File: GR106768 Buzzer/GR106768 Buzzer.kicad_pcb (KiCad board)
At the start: 4 copper layers, 76 x 58 mm, 232 parts, among them IC1 L-BC-SOT23-5, IC2 L-BC-SO08, IC3 L-BC-SO08, IC4 L-BC-SOT23-5, IC5 L-BC-SO08, IC6 L-BC-SO08, IC7 L-BC-SOT23-6, IC8 L-BC-DFN10, IC9 L-BC-SOT23-6, J1 BAR-10-1007, J2 MIRECMS, J3 MIRECMS, SW1 SI-10-NK236, T1 Q-BC-SOT23-BEC, T10 Q-BC-SOT23-GSD, T11 Q-BC-SOT23-GSD, T12 Q-BC-SOT23-GSD, T13 Q-BC-SOT23-GSD, T2 Q-BC-SOT23-BEC, T3 Q-BC-SOT23-BEC, T4 Q-BC-SOT23-BEC, T5 Q-BC-SOT23-GSD, T6 Q-BC-SOT23-GSD, T7 Q-BC-SOT23-GSD, T8 Q-BC-SOT23-GSD, T9 Q-BC-SOT23-GSD

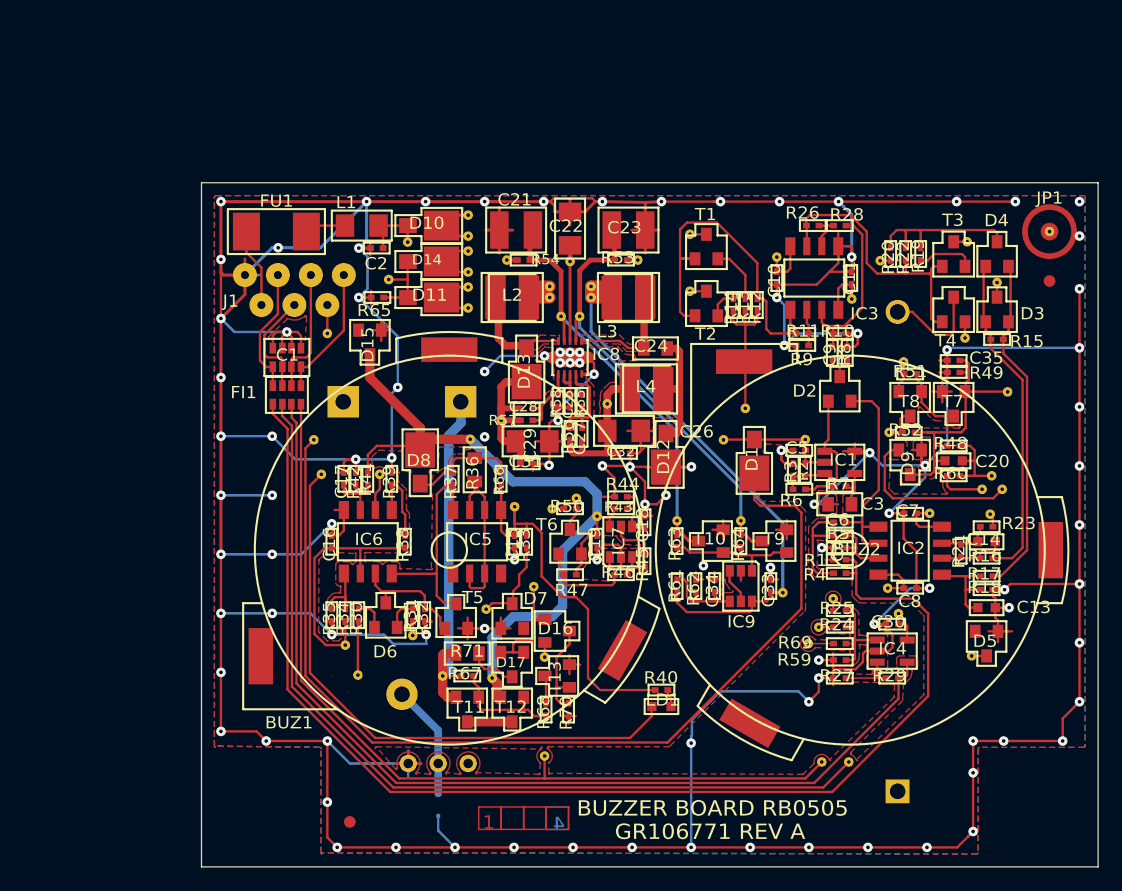
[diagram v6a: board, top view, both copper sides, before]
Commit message: buzzer pcb, schematics, etc.
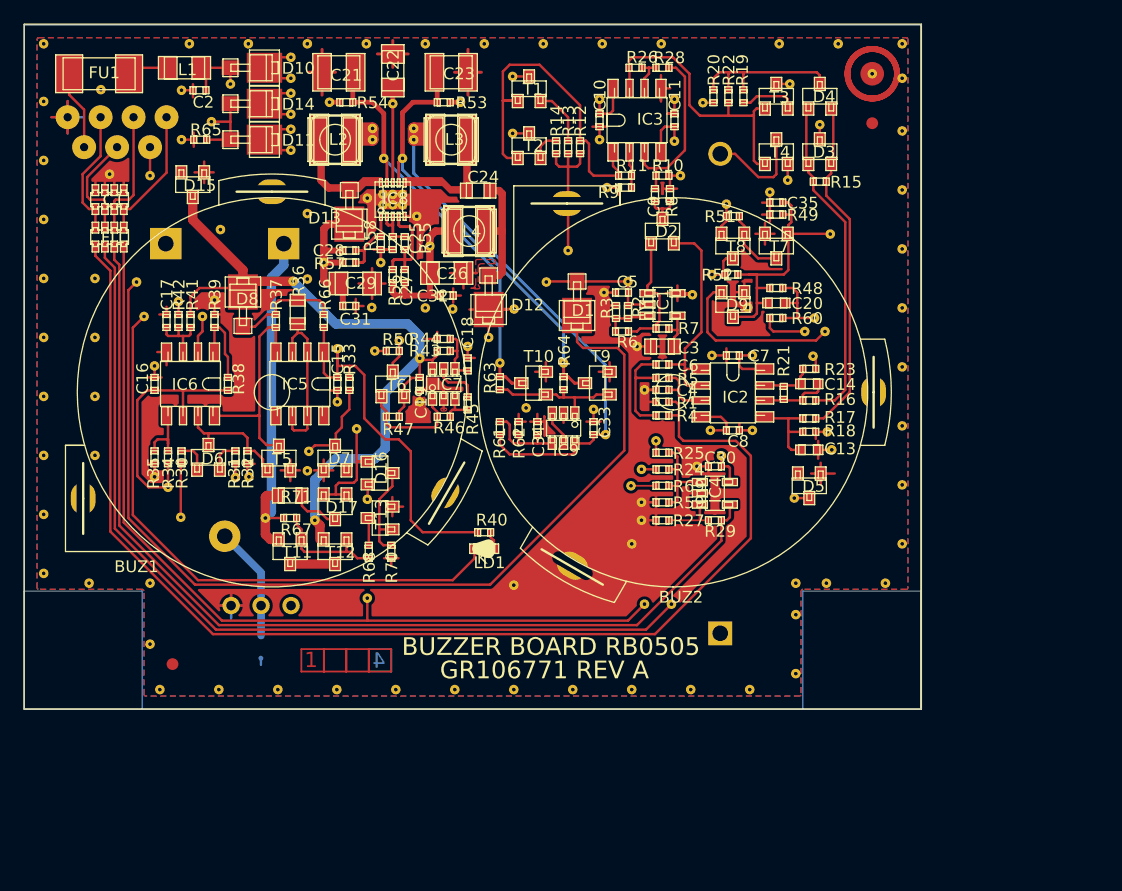
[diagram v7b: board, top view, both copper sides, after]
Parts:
- added V100: VIA-08X03-VE_1011, VIA-08X03-VE_1011, F.Cu at (164.7, 65.2)
- added V101: VIA-08X03-VE, VIA-08X03-VE, F.Cu at (101.7, 63.5)
- added V102: VIA-08X03-VE_1011, VIA-08X03-VE_1011, F.Cu at (122.6, 62.6)
- added V103: VIA-08X03-VE, VIA-08X03-VE, F.Cu at (148.8, 61.7)
- added V104: VIA-08X03-VE_1011, VIA-08X03-VE_1011, F.Cu at (155.1, 61.9)
- added V105: VIA-08X03-VE_1011, VIA-08X03-VE_1011, F.Cu at (122.6, 60.9)
- added V106: VIA-08X03-VE_1011, VIA-08X03-VE_1011, F.Cu at (141.4, 61.2)
- added V107: VIA-08X03-VE, VIA-08X03-VE, F.Cu at (174.4, 61.0)
- added V108: VIA-08X03-VE_1011, VIA-08X03-VE_1011, F.Cu at (115.9, 60.2)
- added V109: VIA-08X03-VE_1011, VIA-08X03-VE_1011, F.Cu at (167.4, 60.5)
- added V110: VIA-08X03-VE_1011, VIA-08X03-VE_1011, F.Cu at (122.6, 59.6)
- added V111: VIA-08X03-VE, VIA-08X03-VE, F.Cu at (101.7, 58.5)
- added V112: VIA-08X03-VE_1011, VIA-08X03-VE_1011, F.Cu at (148.8, 58.3)
- added V113: VIA-08X03-VE, VIA-08X03-VE, F.Cu at (155.1, 58.3)
- added V114: VIA-08X03-VE_1011, VIA-08X03-VE_1011, F.Cu at (157.5, 58.6)
- added V115: VIA-08X03-VE_1011, VIA-08X03-VE_1011, F.Cu at (122.6, 57.8)
- added V116: VIA-08X03-VE, VIA-08X03-VE, F.Cu at (106.5, 57.5)
- added V117: VIA-08X03-VE, VIA-08X03-VE, F.Cu at (113.3, 57.5)
- added V118: VIA-08X03-VE_1011, VIA-08X03-VE_1011, F.Cu at (117.5, 57.0)
- added V119: VIA-08X03-VE_1011, VIA-08X03-VE_1011, F.Cu at (164.9, 57.0)
- added V120: VIA-08X03-VE_1011, VIA-08X03-VE_1011, F.Cu at (122.6, 56.5)
- added V121: VIA-08X03-VE_1011, VIA-08X03-VE_1011, F.Cu at (141.4, 56.4)
- added V122: VIA-08X03-VE_1011, VIA-08X03-VE_1011, F.Cu at (171.9, 56.2)
- added V123: VIA-08X03-VE_1011, VIA-08X03-VE_1011, F.Cu at (122.6, 54.8)
- added V124: VIA-08X03-VE, VIA-08X03-VE, F.Cu at (101.7, 53.6)
- added V125: VIA-08X03-VE, VIA-08X03-VE, F.Cu at (114.0, 53.6)
- added V126: VIA-08X03-VE, VIA-08X03-VE, F.Cu at (119.0, 53.6)
- added V127: VIA-08X03-VE, VIA-08X03-VE, F.Cu at (124.0, 53.6)
- added V128: VIA-08X03-VE, VIA-08X03-VE, F.Cu at (129.0, 53.6)
- added V129: VIA-08X03-VE, VIA-08X03-VE, F.Cu at (134.0, 53.6)
- added V130: VIA-08X03-VE, VIA-08X03-VE, F.Cu at (139.0, 53.6)
- added V131: VIA-08X03-VE, VIA-08X03-VE, F.Cu at (144.0, 53.6)
- added V132: VIA-08X03-VE, VIA-08X03-VE, F.Cu at (149.0, 53.6)
- added V133: VIA-08X03-VE, VIA-08X03-VE, F.Cu at (154.0, 53.6)
- added V134: VIA-08X03-VE, VIA-08X03-VE, F.Cu at (164.0, 53.6)
- added V135: VIA-08X03-VE, VIA-08X03-VE, F.Cu at (169.0, 53.6)
- added V136: VIA-08X03-VE, VIA-08X03-VE, F.Cu at (174.4, 53.6)
- added V137: VIA-08X03-VE, VIA-08X03-VE, F.Cu at (174.4, 56.5)
- added V138: VIA-08X03-VE, VIA-08X03-VE, F.Cu at (161.3, 76.0)
- added V139: VIA-08X03-VE_1011, VIA-08X03-VE_1011, F.Cu at (112.2, 91.2)
- added V140: VIA-08X03-VE, VIA-08X03-VE, F.Cu at (119.0, 90.3)
- added V141: VIA-08X03-VE_1011, VIA-08X03-VE_1011, F.Cu at (146.1, 71.1)
- added V142: VIA-08X03-VE_1011, VIA-08X03-VE_1011, F.Cu at (168.3, 69.7)
- added V143: VIA-08X03-VE, VIA-08X03-VE, F.Cu at (163.2, 66.2)
- added V144: VIA-08X03-VE, VIA-08X03-VE, F.Cu at (151.9, 79.3)
- added V145: VIA-08X03-VE_1011, VIA-08X03-VE_1011, F.Cu at (133.0, 60.8)
- added V146: VIA-08X03-VE_1011, VIA-08X03-VE_1011, F.Cu at (113.3, 93.7)
- added V147: VIA-08X03-VE, VIA-08X03-VE, F.Cu at (124.0, 73.6)
- added V148: VIA-08X03-VE, VIA-08X03-VE, F.Cu at (113.3, 61.7)
- added V149: VIA-08X03-VE_1011, VIA-08X03-VE_1011, F.Cu at (137.0, 58.6)
- added V150: VIA-08X03-VE_1011, VIA-08X03-VE_1011, F.Cu at (131.2, 58.7)
- added V151: VIA-08X03-VE_1011, VIA-08X03-VE_1011, F.Cu at (125.9, 58.6)
- added V152: VIA-08X03-VE_1011, VIA-08X03-VE_1011, F.Cu at (129.5, 60.8)
- added V153: VIA-08X03-VE_1011, VIA-08X03-VE_1011, F.Cu at (129.5, 61.7)
- added V154: VIA-08X03-VE_1011, VIA-08X03-VE_1011, F.Cu at (133.0, 61.7)
- added V155: VIA-08X03-VE_1001, VIA-08X03-VE_1001, F.Cu at (130.5, 63.3)
- added V156: VIA-08X03-VE_1001, VIA-08X03-VE_1001, F.Cu at (132.1, 63.3)
- added V157: VIA-08X03-VE, VIA-08X03-VE, F.Cu at (142.5, 84.5)
- added V158: VIA-08X03-VE, VIA-08X03-VE, F.Cu at (148.3, 84.6)
- added V159: VIA-08X03-VE_1001, VIA-08X03-VE_1001, F.Cu at (149.3, 86.7)
- added V160: VIA-08X03-VE_1001, VIA-08X03-VE_1001, F.Cu at (145.7, 80.7)
- added V161: VIA-08X03-VE_1001, VIA-08X03-VE_1001, F.Cu at (140.3, 80.7)
- added V162: VIA-08X03-VE, VIA-08X03-VE, F.Cu at (116.6, 69.4)
- added V163: VIA-08X03-VE, VIA-08X03-VE, F.Cu at (124.0, 89.8)
- added V164: VIA-08X03-VE_1011, VIA-08X03-VE_1011, F.Cu at (124.1, 88.2)
- added V165: VIA-08X03_1011, VIA-08X03_1011, F.Cu at (124.6, 94.0)
- added V166: VIA-08X03_1011, VIA-08X03_1011, F.Cu at (129.1, 92.2)
- added V167: VIA-08X03_1011, VIA-08X03_1011, F.Cu at (128.2, 86.3)
- added V168: VIA-08X03_1011, VIA-08X03_1011, F.Cu at (129.1, 100.6)
- added V169: VIA-08X03-VE, VIA-08X03-VE, F.Cu at (152.3, 94.0)
- added V170: VIA-08X03-VE, VIA-08X03-VE, F.Cu at (152.3, 92.5)
- added V171: VIA-08X03_1011, VIA-08X03_1011, F.Cu at (151.4, 91.1)
- added V172: VIA-08X03_1001, VIA-08X03_1001, F.Cu at (120.4, 93.8)
- added V173: VIA-08X03_1001, VIA-08X03_1001, F.Cu at (122.8, 73.7)
- added V69: VIA-08X03-VE, VIA-08X03-VE, F.Cu at (113.1, 75.5)
- added V70: VIA-08X03-VE, VIA-08X03-VE, F.Cu at (129.5, 76.0)
- added V71: VIA-08X03-VE, VIA-08X03-VE, F.Cu at (116.1, 75.3)
- added V72: VIA-08X03-VE, VIA-08X03-VE, F.Cu at (156.6, 74.9)
- added V73: VIA-08X03-VE, VIA-08X03-VE, F.Cu at (149.1, 74.7)
- added V74: VIA-08X03-VE, VIA-08X03-VE, F.Cu at (101.7, 73.5)
- added V75: VIA-08X03-VE, VIA-08X03-VE, F.Cu at (106.0, 73.5)
- added V76: VIA-08X03-VE_1011, VIA-08X03-VE_1011, F.Cu at (109.5, 73.8)
- added V77: VIA-08X03-VE_1011, VIA-08X03-VE_1011, F.Cu at (144.3, 73.8)
- added V78: VIA-08X03-VE_1011, VIA-08X03-VE_1011, F.Cu at (151.2, 73.8)
- added V79: VIA-08X03-VE_1011, VIA-08X03-VE_1011, F.Cu at (158.3, 73.2)
- added V80: VIA-08X03-VE_1011, VIA-08X03-VE_1011, F.Cu at (125.4, 72.2)
- added V81: VIA-08X03-VE, VIA-08X03-VE, F.Cu at (130.2, 72.2)
- added V82: VIA-08X03-VE, VIA-08X03-VE, F.Cu at (174.4, 71.0)
- added V83: VIA-08X03-VE_1011, VIA-08X03-VE_1011, F.Cu at (134.4, 70.8)
- added V84: VIA-08X03-VE, VIA-08X03-VE, F.Cu at (101.7, 68.5)
- added V85: VIA-08X03-VE, VIA-08X03-VE, F.Cu at (124.0, 68.0)
- added V86: VIA-08X03-VE, VIA-08X03-VE, F.Cu at (133.3, 68.2)
- added V87: VIA-08X03-VE, VIA-08X03-VE, F.Cu at (130.4, 67.3)
- added V88: VIA-08X03-VE, VIA-08X03-VE, F.Cu at (131.2, 67.3)
- added V89: VIA-08X03-VE, VIA-08X03-VE, F.Cu at (132.1, 67.3)
- added V90: VIA-08X03-VE_1011, VIA-08X03-VE_1011, F.Cu at (159.5, 67.2)
- added V91: VIA-08X03-VE, VIA-08X03-VE, F.Cu at (129.1, 66.7)
- added V92: VIA-08X03-VE, VIA-08X03-VE, F.Cu at (130.4, 66.4)
- added V93: VIA-08X03-VE, VIA-08X03-VE, F.Cu at (131.2, 66.4)
- added V94: VIA-08X03-VE, VIA-08X03-VE, F.Cu at (132.1, 66.4)
- added V95: VIA-08X03-VE, VIA-08X03-VE, F.Cu at (174.4, 66.0)
- added V96: VIA-08X03-VE, VIA-08X03-VE, F.Cu at (149.4, 65.8)
- added V97: VIA-08X03-VE, VIA-08X03-VE, F.Cu at (107.2, 64.7)
- added V98: VIA-08X03-VE_1011, VIA-08X03-VE_1011, F.Cu at (110.7, 64.8)
- added V99: VIA-08X03-VE, VIA-08X03-VE, F.Cu at (155.6, 64.8)
- added cam2: PER-COVIDIEN_TEXTE, AllModules:PER-COVIDIEN_TEXTE, F.Cu at (15.0, 175.0)
- added cam6: COIN_EXTERNE, COIN_EXTERNE, F.Cu at (100.0, 52.0)
- added cam7: COIN_EXTERNE, COIN_EXTERNE, F.Cu at (100.0, 110.0)
- added cam8: COIN_EXTERNE, COIN_EXTERNE, F.Cu at (176.0, 110.0)
- added cam9: COIN_EXTERNE, COIN_EXTERNE, F.Cu at (176.0, 52.0)
- BAT1: footprint BT-4-V150H-4.8V_1 -> BT-4-V150H-4.8V_100110011001
- BUZ1: footprint PKM33EPH-1201C_1 -> PKM33EPH-1201C_101110111001
- BUZ2: footprint PKM33EPH-1201C_1 -> PKM33EPH-1201C_100110111001
- C1: footprint C0612-4_1 -> C0612-4
- C10, C11, C15, C16, C17, C18, C19, C2, C25, C27, C28, C30, C31, C32, C33, C34, C35, C4, C5, C6, C7, C8, C9: footprint C0402_1 -> C0402
- C12: footprint AX10X30_1 -> AX10X30_10111011
- C13, C14, C20: footprint C0603_1 -> C0603
- C21, C23: footprint C1210_1 -> C1210
- C22, C26, C29, L1: footprint RC1206_1 -> RC1206
- C24, C3: footprint C0805_1 -> C0805
- D1, D10, D11, D12, D13, D14, D8: footprint DO216AA_1 -> DO216AA
- D15, D16, D17, D2, D3, D4, D5, D6, D7, D9: footprint SOT23-1G_1 -> SOT23-1G
- FI1: footprint WE-FA_1 -> WE-FA
- FU1: footprint F6126_1 -> F6126
- IC1, IC4: footprint SOT23-5_1 -> SOT23-5
- IC2, IC3, IC5, IC6: footprint MX.A8_COMPOSANT_1 -> MX.A8_COMPOSANT
- IC7, IC9: footprint SOT23-6_1 -> SOT23-6
- IC8: footprint DFN10_1 -> DFN10
- J1: footprint BAR7-3-2-COVIDIEN_1 -> BAR7-3-2-COVIDIEN_1111100110011001100110011001
- J2, J3: footprint MIRECMS-SAFT_1 -> MIRECMS-SAFT
- JP1: footprint TB-CMS-AIROX_1 -> TB-CMS-AIROX
- L2, L3, L4: footprint WETPC-S_1 -> WETPC-S
- L2-2: footprint NR4018_1 -> NR4018
- L3-2, L4-2: footprint NR4012_1 -> NR4012
- LD1: footprint D0603_1 -> D0603
- R1, R10, R11, R12, R13, R14, R15, R16, R17, R18, R19, R2, R20, R21, R22, R23, R24, R25, R26, R27, R28, R29, R3, R30, R31, R32, R33, R34, R35, R37, R38, R39, R4, R40, R41, R42, R43, R44, R45, R46, R47, R48, R49, R5, R50, R51, R52, R53, R54, R55, R56, R57, R58, R59, R6, R60, R61, R62, R63, R64, R65, R66, R67, R68, R69, R7, R70, R8, R9: footprint R0402_1 -> R0402
- R36, R71: footprint R0805_1 -> R0805
- SJ1: footprint TB-CMS-AIROX-2_1 -> TB-CMS-AIROX-2
- SW1: footprint NK236_1_1 -> NK236_1_100110011111
- T1, T2, T3, T4: footprint SOT23-BEC_1 -> SOT23-BEC
- T10, T11, T12, T13, T5, T6, T7, T8, T9: footprint SOT23-GSD_1 -> SOT23-GSD
- V1, V2, V3, V4, V5: value +5V -> VIA-08X03-VE; footprint AllModules:Via_12x32-1._.3.4 -> VIA-08X03-VE
- V10, V11: value SUPPLY-BUZ-CPU -> VIA-08X03-VE; footprint AllModules:Via_12x32-1._.3.4 -> VIA-08X03-VE
- V12, V13, V14: value -12V -> VIA-08X03-VE; footprint AllModules:Via_12x32-1._.3.4 -> VIA-08X03-VE
- V15: value -12V -> VIA-08X03-VE_1011; footprint AllModules:Via_12x32-1._.3.4 -> VIA-08X03-VE_1011
- V16: value N$78 -> VIA-08X03-VE_1011; footprint AllModules:Via_12x32-1._.3.4 -> VIA-08X03-VE_1011
- V17: value N$78 -> VIA-08X03-VE; footprint AllModules:Via_12x32-1._.3.4 -> VIA-08X03-VE
- V18, V19: value N$58 -> VIA-08X03-VE; footprint AllModules:Via_12x32-1._.3.4 -> VIA-08X03-VE
- V20: value N$31 -> VIA-08X03-VE; footprint AllModules:Via_12x32-1._.3.4 -> VIA-08X03-VE
- V21, V22: value GT1 -> VIA-08X03-VE; footprint AllModules:Via_12x32-1._.3.4 -> VIA-08X03-VE
- V23, V24, V25, V26, V28: value +12V -> VIA-08X03-VE; footprint AllModules:Via_12x32-1._.3.4 -> VIA-08X03-VE
- V27: value +12V -> VIA-08X03-VE_1011; footprint AllModules:Via_12x32-1._.3.4 -> VIA-08X03-VE_1011
- V29: value BATTV -> VIA-08X03-VE; footprint AllModules:Via_12x32-1._._.4 -> VIA-08X03-VE
- V30: value N$19 -> VIA-08X03-VE_1011; footprint AllModules:Via_12x32-1._.3.4 -> VIA-08X03-VE_1011
- V31: value N$18 -> VIA-08X03-VE_1011; footprint AllModules:Via_12x32-1._.3.4 -> VIA-08X03-VE_1011
- V32: value N$18 -> VIA-08X03-VE; footprint AllModules:Via_12x32-1._.3.4 -> VIA-08X03-VE
- V33: value N$10 -> VIA-08X03-VE; footprint AllModules:Via_12x32-1._._.4 -> VIA-08X03-VE
- V34, V36, V39, V40, V41, V42, V43, V44, V45, V46: value N$10 -> VIA-08X03-VE; footprint AllModules:Via_12x32-1._.3.4 -> VIA-08X03-VE
- V35, V37, V38: value N$10 -> VIA-08X03-VE_1011; footprint AllModules:Via_12x32-1._.3.4 -> VIA-08X03-VE_1011
- V47, V48: value STOP-INV -> VIA-08X03-VE; footprint AllModules:Via_12x32-1._.3.4 -> VIA-08X03-VE
- V49: value VCHARG -> VIA-08X03-VE_1001; footprint AllModules:Via_12x32-1._._.4 -> VIA-08X03-VE_1001
- V50: value VCHARG -> VIA-08X03-VE; footprint AllModules:Via_12x32-1._.3.4 -> VIA-08X03-VE
- V51: value VCHARG -> VIA-08X03-VE_1011; footprint AllModules:Via_12x32-1._.3.4 -> VIA-08X03-VE_1011
- V52: value VCHARG -> VIA-08X03-VE_1011; footprint AllModules:Via_12x32-1._._.4 -> VIA-08X03-VE_1011
- V53, V54: value VBAT -> VIA-08X03-VE_1011; footprint AllModules:Via_12x32-1._.3.4 -> VIA-08X03-VE_1011
- V55: value VBAT -> VIA-08X03-VE; footprint AllModules:Via_12x32-1._.3.4 -> VIA-08X03-VE
- V56, V57, V59: value SUPPLY-BUZ -> VIA-08X03-VE; footprint AllModules:Via_12x32-1._.3.4 -> VIA-08X03-VE
- V58, V60: value SUPPLY-BUZ -> VIA-08X03-VE_1011; footprint AllModules:Via_12x32-1._.3.4 -> VIA-08X03-VE_1011
- V6, V7, V8, V9: value BUZ-ACT -> VIA-08X03-VE; footprint AllModules:Via_12x32-1._.3.4 -> VIA-08X03-VE
- V61, V62: value SHDN2 -> VIA-08X03-VE_1011; footprint AllModules:Via_12x32-1._._.4 -> VIA-08X03-VE_1011
- V63, V64: value SHDN1 -> VIA-08X03-VE_1011; footprint AllModules:Via_12x32-1._._.4 -> VIA-08X03-VE_1011
- V65, V66, V67, V68: value INHIB-STOP-INV -> VIA-08X03-VE; footprint AllModules:Via_12x32-1._.3.4 -> VIA-08X03-VE
- moved V47 71.6 mm to (111.0, 80.9)
- moved V57 67.8 mm to (106.0, 78.5)
- moved V13 66.3 mm to (110.7, 104.5)
- moved V33 63.7 mm to (101.7, 88.5)
- moved V3 62.1 mm to (121.5, 108.3)
- moved V23 61.9 mm to (101.7, 98.5)
- moved V53 48.0 mm to (126.5, 79.5)
- moved V34 44.1 mm to (106.0, 88.5)
- moved V67 44.1 mm to (141.5, 76.1)
- moved V63 43.8 mm to (115.1, 76.7)
- moved V30 43.6 mm to (117.9, 90.4)
- moved V10 43.1 mm to (156.5, 108.3)
- moved V5 43.1 mm to (131.5, 108.3)
- moved V7 43.0 mm to (141.5, 108.3)
- moved V11 42.6 mm to (161.5, 108.3)
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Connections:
- net +5V_CPU renamed /+5V_CPU
- net INHIB-STOP-INV-CPU renamed /INHIB-STOP-INV-CPU
- net N$1 renamed /N$1
- net N$11 renamed /N$11
- net N$12 renamed /N$12
- net N$13 renamed /N$13
- net N$14 renamed /N$14
- net N$15 renamed /N$15
- net N$16 renamed /N$16
- net N$17 renamed /N$17
- net N$2 renamed /N$2
- net N$20 renamed /N$20
- net N$21 renamed /N$21
- net N$22 renamed /N$22
- net N$23 renamed /N$23
- net N$24 renamed /N$24
- net N$25 renamed /N$25
- net N$26 renamed /N$26
- net N$27 renamed /N$27
- net N$28 renamed /N$28
- net N$29 renamed /N$29
- net N$3 renamed /N$3
- net N$30 renamed /N$30
- net N$32 renamed /N$32
- net N$33 renamed /N$33
- net N$34 renamed /N$34
- net N$35 renamed /N$35
- net N$36 renamed /N$36
- net N$37 renamed /N$37
- net N$38 renamed /N$38
- net N$39 renamed /N$39
- net N$4 renamed /N$4
- net N$40 renamed /N$40
- net N$41 renamed /N$41
- net N$42 renamed /N$42
- net N$43 renamed /N$43
- net N$44 renamed /N$44
- net N$45 renamed /N$45
- net N$46 renamed /N$46
- net N$47 renamed /N$47
- net N$48 renamed /N$48
- net N$49 renamed /N$49
- net N$5 renamed /N$5
- net N$50 renamed /N$50
- net N$51 renamed /N$51
- net N$52 renamed /N$52
- net N$53 renamed /N$53
- net N$54 renamed /N$54
- net N$55 renamed /N$55
- net N$56 renamed /N$56
- net N$57 renamed /N$57
- net N$59 renamed /N$59
- net N$6 renamed /N$6
- net N$7 renamed /N$7
- net N$8 renamed /N$8
- net N$9 renamed /N$9
- net PWM-BUZ renamed /PWM-BUZ
- net PWM-BUZZER-CPU renamed /PWM-BUZZER-CPU
- net STOP-INV-CPU renamed /STOP-INV-CPU
- net TEST-BUZZER-CPU renamed /TEST-BUZZER-CPU
- net TESTBUZ renamed /TESTBUZ
- BAT1 pad +: BATTV -> /BATTV
- BUZ1 pad 1: N$19 -> /N$19
- BUZ1 pad 2: N$31 -> /N$31
- BUZ2 pad 1: N$19 -> /N$19
- BUZ2 pad 2: N$31 -> /N$31
- C10 pad 2: +12V -> /+12V
- C11 pad 2: -12V -> /-12V
- C12 pad +: +12V -> /+12V
- C12 pad -: -12V -> /-12V
- C15 pad 2: +12V -> /+12V
- C16 pad 1: N$58 -> /N$58
- C19 pad 1: VCHARG -> /VCHARG
- C2 pad 2: +5V -> /+5V
- C20 pad 1: GT1 -> /GT1
- C20 pad 2: STOP-INV -> /STOP-INV
- C21 pad 2: SHDN1 -> /SHDN1
- C22 pad 1: N$10 -> /N$10
- C23 pad 2: SHDN2 -> /SHDN2
- C26 pad 1: -12V -> /-12V
- C27 pad 1: -12V -> /-12V
- C28 pad 2: +12V -> /+12V
- C29 pad 2: +12V -> /+12V
- C30 pad 1: +5V -> /+5V
- C31 pad 2: +12V -> /+12V
- C32 pad 2: -12V -> /-12V
- C33 pad 1: N$10 -> /N$10
- C35 pad 2: GT1 -> /GT1
- C5 pad 1: SUPPLY-BUZ -> /SUPPLY-BUZ
- C7 pad 1: +12V -> /+12V
- C8 pad 1: -12V -> /-12V
- D1 pad A: SUPPLY-BUZ -> /SUPPLY-BUZ
- D1 pad K: SUPPLY-BUZ-CPU -> /SUPPLY-BUZ-CPU
- D10 pad A: +5V -> /+5V
- D10 pad K: N$10 -> /N$10
- D11 pad A: SUPPLY-BUZ -> /SUPPLY-BUZ
- D11 pad K: N$10 -> /N$10
- D13 pad K: +12V -> /+12V
- D14 pad A: SUPPLY-BUZ -> /SUPPLY-BUZ
- D14 pad K: N$10 -> /N$10
- D15 pad 3: VCHARG -> /VCHARG
- D16 pad 1: +5V -> /+5V
- D16 pad 2: INHIB-STOP-INV -> /INHIB-STOP-INV
- D17 pad 1: +5V -> /+5V
- D17 pad 2: +5V -> /+5V
- D3 pad 3: N$31 -> /N$31
- D5 pad 3: BUZ-ACT -> /BUZ-ACT
- D7 pad 3: N$58 -> /N$58
- D8 pad K: VCHARG -> /VCHARG
- D9 pad 2: INHIB-STOP-INV -> /INHIB-STOP-INV
- D9 pad 3: GT1 -> /GT1
- FI1 pad L2A: STOP-INV -> /STOP-INV
- FI1 pad L4A: INHIB-STOP-INV -> /INHIB-STOP-INV
- IC1 pad 2: SUPPLY-BUZ -> /SUPPLY-BUZ
- IC2 pad 4: -12V -> /-12V
- IC2 pad 8: +12V -> /+12V
- IC3 pad 4: -12V -> /-12V
- IC3 pad 8: +12V -> /+12V
- IC4 pad 5: +5V -> /+5V
- IC5 pad 1: +12V -> /+12V
- IC6 pad 2: N$78 -> /N$78
- IC6 pad 6: N$58 -> /N$58
- IC7 pad 6: VCHARG -> /VCHARG
- IC8 pad 7: SHDN2 -> /SHDN2
- IC8 pad 8: N$10 -> /N$10
- IC8 pad 9: SHDN1 -> /SHDN1
- IC9 pad 6: N$10 -> /N$10
- J1 pad 6: SUPPLY-BUZ-CPU -> /SUPPLY-BUZ-CPU
- JP1 pad 2: GT1 -> /GT1
- L1 pad 2: +5V -> /+5V
- L2 pad 1: N$10 -> /N$10
- L2-2 pad 1: N$10 -> /N$10
- L3 pad 1: N$10 -> /N$10
- L3-2 pad 1: N$10 -> /N$10
- L4 pad 2: -12V -> /-12V
- L4-2 pad 2: -12V -> /-12V
- LD1 pad K: N$78 -> /N$78
- R12 pad 2: N$19 -> /N$19
- R13 pad 1: N$19 -> /N$19
- R14 pad 2: N$19 -> /N$19
- R2 pad 2: SUPPLY-BUZ -> /SUPPLY-BUZ
- R20 pad 1: N$18 -> /N$18
- R23 pad 2: BUZ-ACT -> /BUZ-ACT
- R24 pad 2: BUZ-ACT -> /BUZ-ACT
- R25 pad 2: VBAT -> /VBAT
- R30 pad 1: BUZ-ACT -> /BUZ-ACT
- R31 pad 1: SUPPLY-BUZ -> /SUPPLY-BUZ
- R33 pad 1: N$58 -> /N$58
- R33 pad 2: +12V -> /+12V
- R34 pad 2: N$58 -> /N$58
- R38 pad 2: N$58 -> /N$58
- R40 pad 1: +12V -> /+12V
- R41 pad 1: VCHARG -> /VCHARG
- R43 pad 2: VCHARG -> /VCHARG
- R47 pad 2: VCHARG -> /VCHARG
- R48 pad 1: STOP-INV -> /STOP-INV
- R48 pad 2: GT1 -> /GT1
- R49 pad 2: GT1 -> /GT1
- R50 pad 1: VBAT -> /VBAT
- R50 pad 2: +5V -> /+5V
- R51 pad 2: VBAT -> /VBAT
- R52 pad 1: GT1 -> /GT1
- R52 pad 2: SUPPLY-BUZ -> /SUPPLY-BUZ
- R53 pad 1: N$10 -> /N$10
- R53 pad 2: SHDN2 -> /SHDN2
- R54 pad 1: N$10 -> /N$10
- R54 pad 2: SHDN1 -> /SHDN1
- R56 pad 2: -12V -> /-12V
- R57 pad 1: +12V -> /+12V
- R60 pad 1: STOP-INV -> /STOP-INV
- R60 pad 2: +5V -> /+5V
- R61 pad 2: N$10 -> /N$10
- R63 pad 2: SHDN1 -> /SHDN1
- R64 pad 2: SHDN2 -> /SHDN2
- R65 pad 2: SUPPLY-BUZ -> /SUPPLY-BUZ
- R66 pad 2: +12V -> /+12V
- R67 pad 2: BATTV -> /BATTV
- R69 pad 1: VCHARG -> /VCHARG
- R71 pad 2: BATTV -> /BATTV
- T1 pad C: +12V -> /+12V
- T10 pad D: SHDN1 -> /SHDN1
- T11 pad S: BATTV -> /BATTV
- T12 pad S: VCHARG -> /VCHARG
- T2 pad C: -12V -> /-12V
- T3 pad C: +12V -> /+12V
- T4 pad C: -12V -> /-12V
- T4 pad E: N$18 -> /N$18
- T6 pad D: VBAT -> /VBAT
- T6 pad S: VCHARG -> /VCHARG
- T7 pad G: GT1 -> /GT1
- T8 pad D: SUPPLY-BUZ -> /SUPPLY-BUZ
- T8 pad S: VBAT -> /VBAT
- T9 pad D: SHDN2 -> /SHDN2
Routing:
- net GND: track 787.5 -> 465.3 mm, vias 105 -> 0
- net +12V: track 195.6 -> 0.00 mm
- net /+12V: track 0.00 -> 195.6 mm
- net +5V: track 138.3 -> 0.00 mm
- net /+5V: track 0.00 -> 138.2 mm
- net /INHIB-STOP-INV: track 0.00 -> 131.1 mm
- net INHIB-STOP-INV: track 131.1 -> 0.00 mm
- net STOP-INV: track 116.7 -> 0.00 mm
- net /STOP-INV: track 0.00 -> 116.7 mm
- net N$10: track 110.3 -> 0.00 mm
- net /N$10: track 0.00 -> 98.6 mm
- net VCHARG: track 98.1 -> 0.00 mm
- net /VCHARG: track 0.00 -> 98.1 mm
- net SUPPLY-BUZ: track 97.1 -> 0.00 mm
- net /SUPPLY-BUZ: track 0.00 -> 97.0 mm
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- removed copper zone on F.Cu, net /N$42
- removed copper zone on F.Cu, net /N$46
- removed copper zone on In2.Cu, net N$10
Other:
- rule trace_min: 0.2 -> 0.1
- board text added: "(1)"
- board text added: "(1) Arraser les pattes des buzzers Respecter la cote de hauteur de cablage des buzzers. Voir plan 40966.E04.000. (1) Level off the buzzer's pins Respect the height dimension for buzzers assembling. Refer to drawing 40966.E04.000."
- board text added: "(1) Fabrique suivant IPC A610 classe III. (1) Manufactured according to IPC A610 class III."
- board text added: "(2)Le fabricant doit etre reconnu UL et doit apposer le marquage correspondant. (2) The manufacturer must be recognized UL and must affix corresponding marking."
- board text added: "+0.10 -0.10"
- board text added: "11.50"
- board text added: "15"
- board text added: "17.00"
- board text added: "18.55"
- board text added: "2.0"
- board text added: "21.00"
- board text added: "25.5"
- board text added: "3.68"
- board text added: "3.81"
- board text added: "31.15"
- board text added: "34.00"
- board text added: "58.00"
- board text added: "7 brins AWG 34 lg 60 +/-2mm"
- board text added: "7 fils blanc UL 1061 AWG26"
- board text added: "7 stands AWG 34 length 60 +/-2mm"
- board text added: "7 white wire UL 1061 AWG26"
- board text added: "7.5"
- board text added: "7.84"
- board text added: "76.00"
- board text added: "9.79"
- board text added: "ATTENTION: Le circuit imprime doit etre UL94V-0. WARNING: The printed circuit board must be UL94V-0."
- board text added: "BAT1"
- board text added: "BUZ1"
- board text added: "BUZ2"
- board text added: "C1"
- board text added: "C10"
- board text added: "C11"
- board text added: "C12"
- board text added: "C12 et BAT1 doivent etre colles. Voir plan 40966.E04.000. C12 and BAT1 must be stuck. Refer to drawing 40966.E04.000."
- board text added: "C13"
- board text added: "C14"
- board text added: "C15"
- board text added: "C16"
- board text added: "C17"
- board text added: "C18"
- board text added: "C19"
- board text added: "C2"
- board text added: "C20"
- board text added: "C21"
- board text added: "C22"
- board text added: "C23"
- board text added: "C24"
- board text added: "C25"
- board text added: "C26"
- board text added: "C27"
- board text added: "C28"
- board text added: "C29"
- board text added: "C3"
- board text added: "C30"
- board text added: "C31"
- board text added: "C32"
- board text added: "C33"
- board text added: "C34"
- board text added: "C35"
- board text added: "C4"
- board text added: "C5"
- board text added: "C6"
- board text added: "C7"
- board text added: "C8"
- board text added: "C9"
- board text added: "Connecteur JST fem modele ZHR 7"
- board text added: "D1"
- board text added: "D10"
- board text added: "D11"
- board text added: "D12"
- board text added: "D13"
- board text added: "D14"
- board text added: "D15"
- board text added: "D16"
- board text added: "D17"
- board text added: "D2"
- board text added: "D3"
- board text added: "D4"
- board text added: "D5"
- board text added: "D6"
- board text added: "D7"
- board text added: "D8"
- board text added: "D9"
- board text added: "FI1"
- board text added: "FU1"
- board text added: "Fabrique suivant IPC A610 classe III. Manufactured according to IPC A610 class III."
- board text added: "Fabrique suivant IPC A610 classe III. Manufactured according to IPC A610 classe III."
- board text added: "Fils colle par colle Scotch Weld ref: 7838 B/A Wires stuck with Scotch Weld glue ref : 7838 B/A"
- board text added: "IC1"
- board text added: "IC2"
- board text added: "IC3"
- board text added: "IC4"
- board text added: "IC5"
- board text added: "IC6"
- board text added: "IC7"
- board text added: "IC8"
- board text added: "IC9"
- board text added: "J1"
- board text added: "J2"
- board text added: "J3"
- board text added: "JP1"
- board text added: "JST female connector modele ZHR 7"
- board text added: "L1"
- board text added: "L2"
- board text added: "L2-2"
- board text added: "L3"
- board text added: "L3-2"
- board text added: "L4"
- board text added: "L4-2"
- board text added: "LD1"
- board text added: "R1"
- board text added: "R10"
- board text added: "R11"
- board text added: "R12"
- board text added: "R13"
- board text added: "R14"
- board text added: "R15"
- board text added: "R16"
- board text added: "R17"
- board text added: "R18"
- board text added: "R19"
- board text added: "R2"
- board text added: "R20"
- board text added: "R21"
- board text added: "R22"
- board text added: "R23"
- board text added: "R24"
- board text added: "R25"
- board text added: "R26"
- board text added: "R27"
- board text added: "R28"
- board text added: "R29"
- board text added: "R3"
- board text added: "R30"
- board text added: "R31"
- board text added: "R32"
- board text added: "R33"
- board text added: "R34"
- board text added: "R35"
- board text added: "R36"
- board text added: "R37"
- board text added: "R38"
- board text added: "R39"
- board text added: "R4"
- board text added: "R40"
- board text added: "R41"
- board text added: "R42"
- board text added: "R43"
- board text added: "R44"
- board text added: "R45"
- board text added: "R46"
- board text added: "R47"
- board text added: "R48"
- board text added: "R49"
- board text added: "R5"
- board text added: "R50"
- board text added: "R51"
- board text added: "R52"
- board text added: "R53"
- board text added: "R54"
- board text added: "R55"
- board text added: "R56"
- board text added: "R57"
- board text added: "R58"
- board text added: "R59"
- board text added: "R6"
- board text added: "R60"
- board text added: "R61"
- board text added: "R62"
- board text added: "R63"
- board text added: "R64"
- board text added: "R65"
- board text added: "R66"
- board text added: "R67"
- board text added: "R68"
- board text added: "R69"
- board text added: "R7"
- board text added: "R70"
- board text added: "R71"
- board text added: "R8"
- board text added: "R9"
- board text added: "SJ1"
- board text added: "SW1"
- board text added: "T1"
- board text added: "T10"
- board text added: "T11"
- board text added: "T12"
- board text added: "T13"
- board text added: "T2"
- board text added: "T3"
- board text added: "T4"
- board text added: "T5"
- board text added: "T6"
- board text added: "T7"
- board text added: "T8"
- board text added: "T9"
- board text added: "Toutes les dimensions sont en millimetre. All the dimensions are in millimeter."
- board text added: "Zone de positionnement de l'etiquette de tracabilite (12x25mm) Traceability label positionning zone (12x25mm)"
- board text added: "cam1"
- board text added: "cam14"
- board text added: "cam3"
- board text added: "cam5"
- board text added: "cam6"
- board text added: "cam7"
- board text added: "cam8"
- board text added: "cam9"
- board text added: "contact SZH-002T-P0.5"

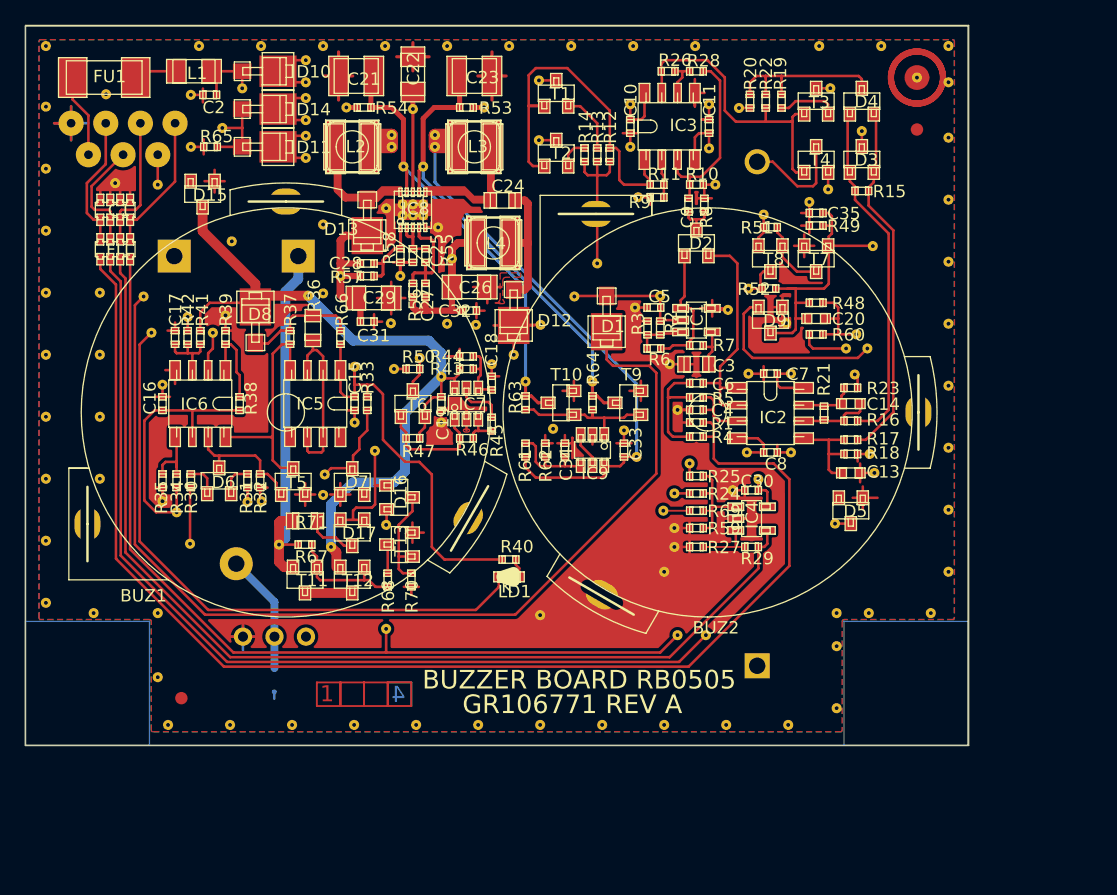
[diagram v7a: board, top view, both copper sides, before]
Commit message: buzzer PCB updated, started on vias
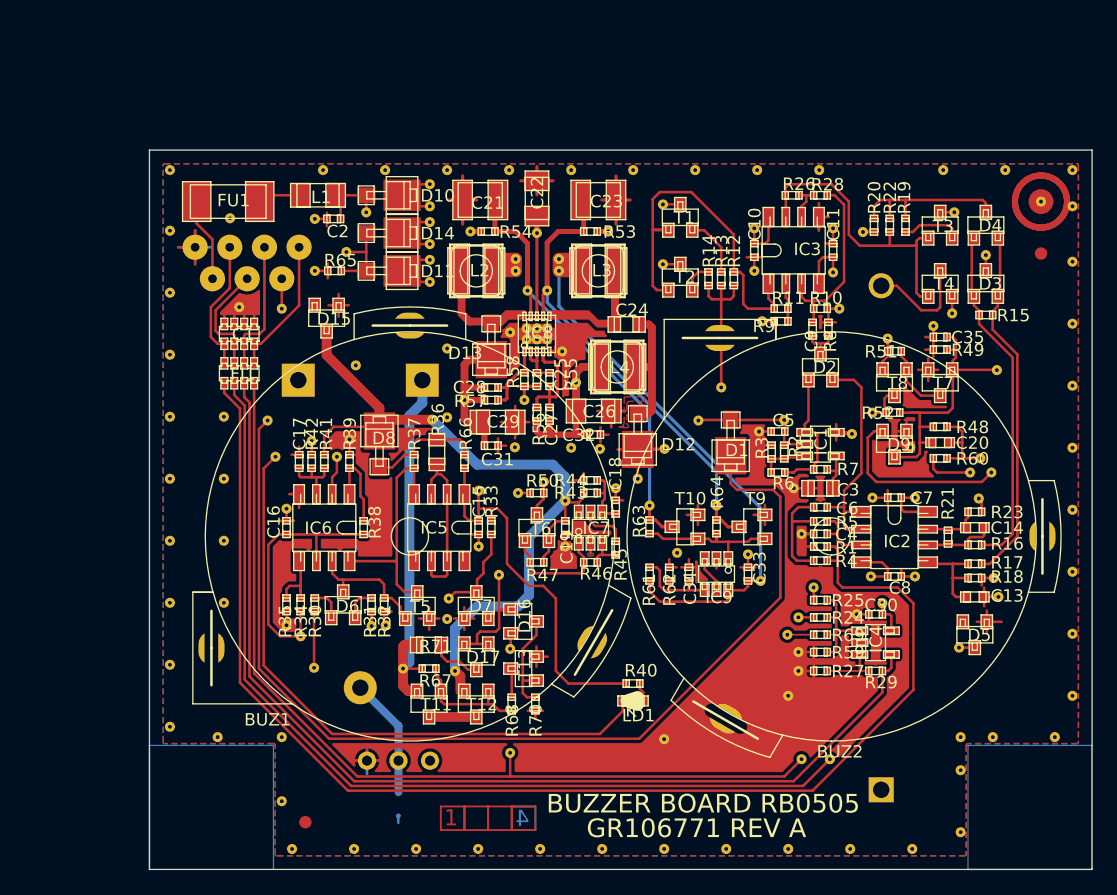
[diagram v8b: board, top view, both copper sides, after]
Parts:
- moved R36 14.1 mm to (133.2, 86.3)
- moved R37 14.1 mm to (131.3, 87.1)
- moved SW1 14.1 mm to (130.1, 111.2)
- moved V140 14.1 mm to (129.1, 100.3)
- moved V173 14.1 mm to (132.8, 83.7)
- moved C2 14.1 mm to (124.9, 67.5)
- moved C23 14.1 mm to (146.2, 66.0)
- moved D10 14.1 mm to (128.9, 65.6)
- moved L1 14.1 mm to (123.6, 65.6)
- moved R26 14.1 mm to (161.8, 65.6)
- moved R28 14.1 mm to (164.1, 65.6)
- moved T2 14.1 mm to (152.8, 72.2)
- moved V102 14.1 mm to (132.6, 72.6)
- moved V104 14.1 mm to (165.1, 71.9)
- moved V112 14.1 mm to (158.8, 68.3)
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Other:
- board text added: "7 strands AWG 34 length 60 +/-2mm"
- board text added: "7 white wires UL 1061 AWG26"
- board text added: "C12 et BAT1 doivent etre colles. Voir plan 40966.E04.000. C12 and BAT1 must be glued. Refer to drawing 40966.E04.000."
- board text added: "JST female connector model ZHR 7"
- board text removed: "7 stands AWG 34 length 60 +/-2mm"
- board text removed: "7 white wire UL 1061 AWG26"
- board text removed: "C12 et BAT1 doivent etre colles. Voir plan 40966.E04.000. C12 and BAT1 must be stuck. Refer to drawing 40966.E04.000."
- board text removed: "JST female connector modele ZHR 7"
